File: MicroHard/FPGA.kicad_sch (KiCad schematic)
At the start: 0 parts

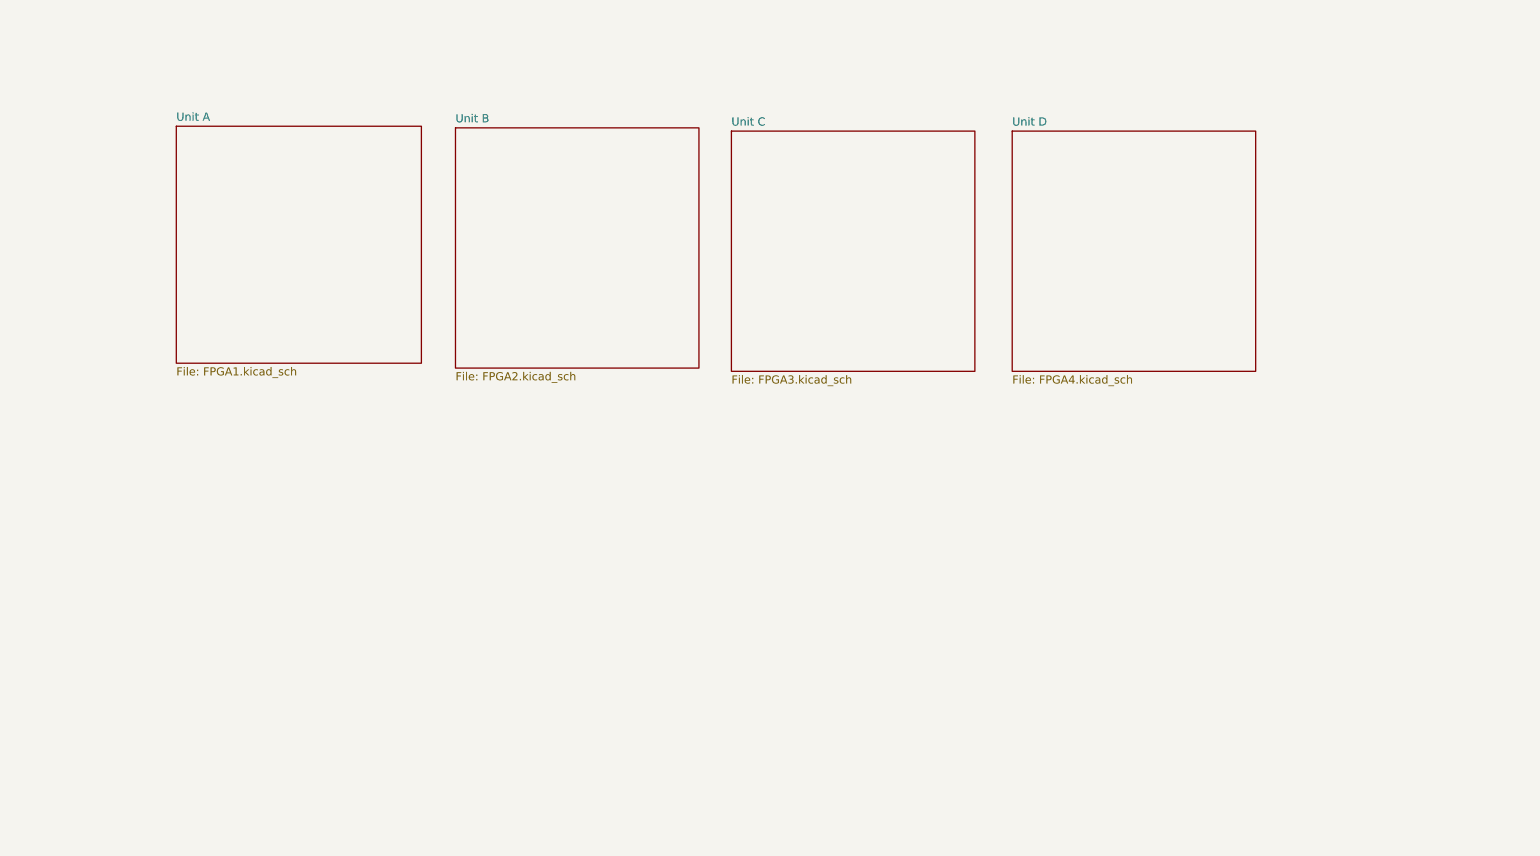
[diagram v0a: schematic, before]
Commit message: feat: finished FPGA config
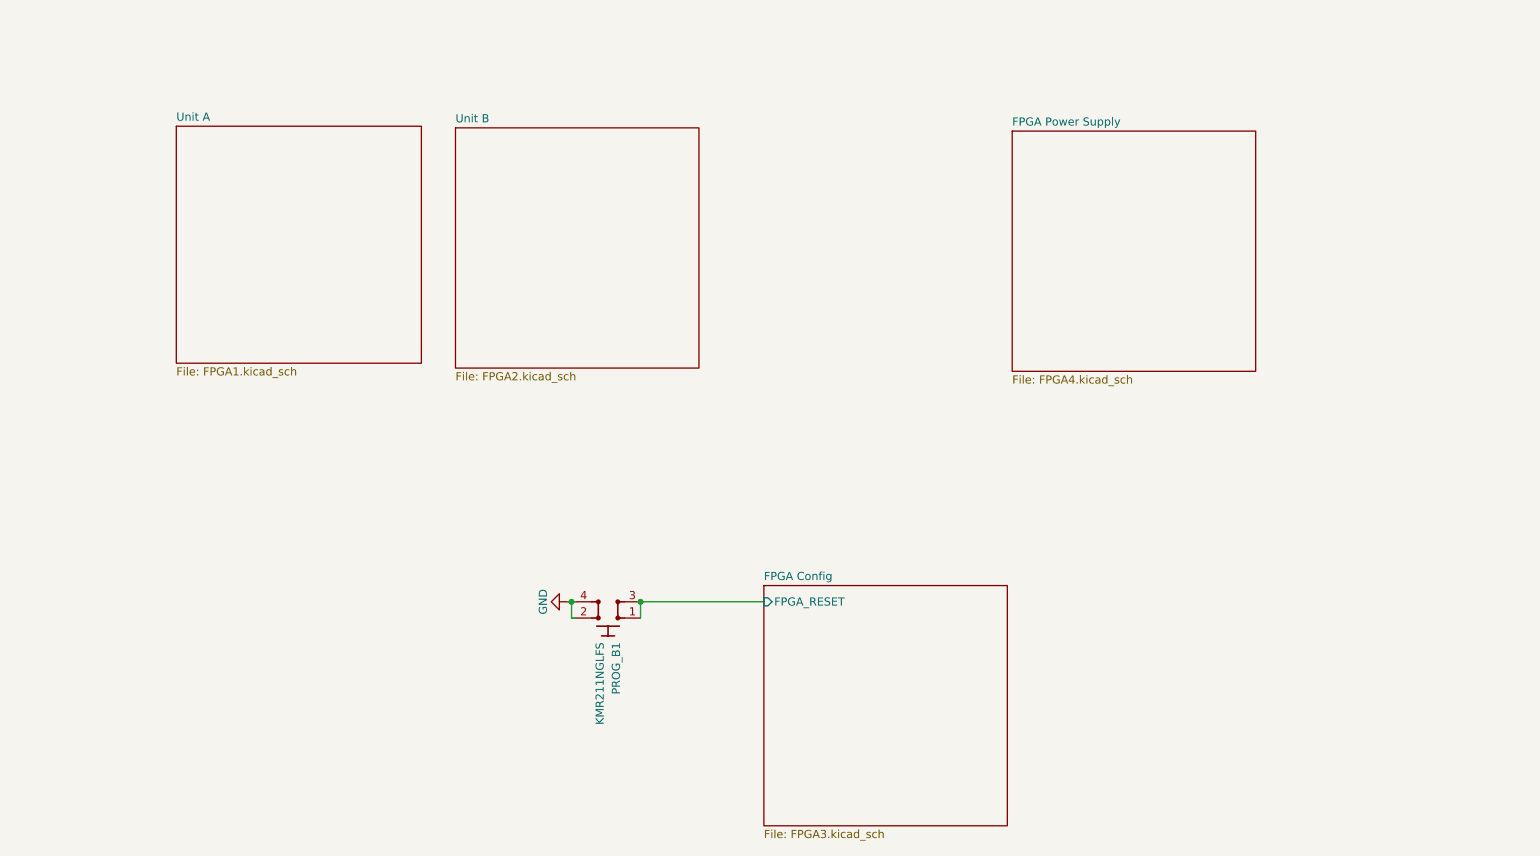
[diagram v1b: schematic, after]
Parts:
- added PROG_B1: SW_SPST_KMR211NGLFS, antmicro-footprints:SW_SPST_4.2x2.8, symbol antmicroPushbuttonSwitches:SW_SPST_KMR211NGLFS
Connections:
- new net FPGA Config/FPGA_RESET: PROG_B1.1, PROG_B1.3
- new net GND: PROG_B1.2, PROG_B1.4
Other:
- sheet Unit C renamed FPGA Config
- sheet Unit D renamed FPGA Power Supply
- sheet FPGA Config ports: added FPGA_RESET; removed none

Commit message: feat: finished Flash mem and FPGA Config
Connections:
- net FPGA Config/FPGA_RESET renamed FPGA_RESET
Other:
- sheet FPGA Config ports: added FPGA_CONFIG_CLOCK; removed none
- sheet Unit A ports: added FPGA_CONFIG_CLOCK; removed none
- note added: "Active Low Full Chip Reset"
- moved on the sheet: PROG_B1
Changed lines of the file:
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@@
 	(paper "A4")
 	(junction
-		(at 94.615 115.57)
+		(at 46.99 113.03)
 		(diameter 0)
 		(color 0 0 0 0)
 	)
 	(junction
-		(at 105.41 115.57)
+		(at 26.035 113.03)
 		(diameter 0)
 		(color 0 0 0 0)
 	)
-	(wire
-		(pts
-			(xy 94.615 118.11) (xy 95.25 118.11)
-		)
-		(stroke
-			(width 0)
-			(type default)
-		)
-	)
-	(wire
-		(pts
-			(xy 94.615 115.57) (xy 95.25 115.57)
-		)
-		(stroke
-			(width 0)
-			(type default)
-		)
-	)
-	(wire
-		(pts
-			(xy 105.41 115.57) (xy 124.714 115.57)
-		)
-		(stroke
-			(width 0)
-			(type default)
-		)
-	)
-	(wire
-		(pts
-			(xy 105.41 115.57) (xy 105.41 118.11)
-		)
-		(stroke
-			(width 0)
-			(type default)
-		)
-	)
-	(wire
-		(pts
-			(xy 94.615 118.11) (xy 94.615 115.57)
-		)
-		(stroke
-			(width 0)
-			(type default)
-		)
-	)
-	(wire
-		(pts
-			(xy 94.615 115.57) (xy 93.98 115.57)
-		)
-		(stroke
-			(width 0)
-			(type default)
+	(junction
+		(at 36.83 113.03)
+		(diameter 0)
+		(color 0 0 0 0)
+	)
+	(junction
+		(at 115.316 114.3)
+		(diameter 0)
+		(color 0 0 0 0)
+	)
+	(wire
+		(pts
+			(xy 57.15 113.03) (xy 46.99 113.03)
+		)
+		(stroke
+			(width 0)
+			(type default)
+		)
+	)
+	(wire
+		(pts
+			(xy 26.035 115.57) (xy 26.67 115.57)
+		)
+		(stroke
+			(width 0)
+			(type default)
+		)
+	)
+	(wire
+		(pts
+			(xy 26.035 113.03) (xy 26.67 113.03)
+		)
+		(stroke
+			(width 0)
+			(type default)
+		)
+	)
+	(wire
+		(pts
+			(xy 36.83 113.03) (xy 46.99 113.03)
+		)
+		(stroke
+			(width 0)
+			(type default)
+		)
+	)
+	(wire
+		(pts
+			(xy 115.316 114.3) (xy 115.57 114.3)
+		)
+		(stroke
+			(width 0)
+			(type default)
+		)
+	)
+	(wire
+		(pts
+			(xy 46.99 105.41) (xy 46.99 113.03)
+		)
+		(stroke
+			(width 0)
+			(type default)
+		)
+	)
+	(wire
+		(pts
+			(xy 36.83 113.03) (xy 36.83 115.57)
+		)
+		(stroke
+			(width 0)
+			(type default)
+		)
+	)
+	(wire
+		(pts
+			(xy 95.25 114.3) (xy 115.316 114.3)
+		)
+		(stroke
+			(width 0)
+			(type default)
+		)
+	)
+	(wire
+		(pts
+			(xy 57.15 113.03) (xy 57.15 114.3)
+		)
+		(stroke
+			(width 0)
+			(type default)
+		)
+	)
+	(wire
+		(pts
+			(xy 26.035 115.57) (xy 26.035 113.03)
+		)
+		(stroke
+			(width 0)
+			(type default)
+		)
+	)
+	(wire
+		(pts
+			(xy 26.035 113.03) (xy 25.4 113.03)
+		)
+		(stroke
+			(width 0)
+			(type default)
+		)
+	)
+	(text "Active Low Full Chip Reset"
+		(exclude_from_sim no)
+		(at 62.484 98.552 0)
+		(effects
+			(font
+				(size 1.27 1.27)
+			)
+		)
+	)
+	(global_label "FPGA_RESET"
+		(shape input)
+		(at 46.99 105.41 90)
+		(fields_autoplaced yes)
+		(effects
+			(font
+				(size 1.27 1.27)
+			)
+			(justify left)
+		)
+		(property "Intersheetrefs" "${INTERSHEET_REFS}"
+			(at 46.99 90.9949 90)
+			(effects
+				(font
+					(size 1.27 1.27)
+				)
+				(justify left)
+				(hide yes)
+			)
 		)
 	)
 	(symbol
 		(lib_id "antmicroPushbuttonSwitches:SW_SPST_KMR211NGLFS")
-		(at 105.41 118.11 180)
+		(at 36.83 115.57 180)
 		(unit 1)
 		(exclude_from_sim no)
@@
 		(fields_autoplaced yes)
 		(property "Reference" "PROG_B1"
-			(at 101.6001 121.92 90)
+			(at 33.0201 119.38 90)
 			(effects
 				(font
@@
 		)
 		(property "Value" "SW_SPST_KMR211NGLFS"
-			(at 99.0601 121.92 90)
+			(at 30.4801 119.38 90)
 			(effects
 				(font
@@
 		)
 		(property "Footprint" "antmicro-footprints:SW_SPST_4.2x2.8"
-			(at 80.01 110.49 0)
+			(at 11.43 107.95 0)
 			(effects
 				(font
@@
 		)
 		(property "Datasheet" "http://www.farnell.com/datasheets/2631211.pdf"
-			(at 80.01 107.95 0)
+			(at 11.43 105.41 0)
 			(effects
 				(font
@@
 		)
 		(property "Description" ""
-			(at 105.41 118.11 0)
+			(at 36.83 115.57 0)
 			(effects
 				(font
@@
 		)
 		(property "MPN" "KMR211NGLFS"
-			(at 99.0601 121.92 90)
+			(at 30.4801 119.38 90)
 			(effects
 				(font
@@
 		)
 		(property "Manufacturer" "C&K"
-			(at 80.01 102.87 0)
+			(at 11.43 100.33 0)
 			(effects
 				(font
@@
 		)
 		(property "Author" "Antmicro"
-			(at 80.01 100.33 0)
+			(at 11.43 97.79 0)
 			(effects
 				(font
@@
 		)
 		(property "License" "Apache-2.0"
-			(at 80.01 97.79 0)
+			(at 11.43 95.25 0)
 			(effects
 				(font
@@
 	(symbol
 		(lib_id "antmicropower:GND")
-		(at 93.98 115.57 270)
+		(at 25.4 113.03 270)
 		(unit 1)
 		(exclude_from_sim no)
@@
 		(dnp no)
 		(property "Reference" "#PWR018"
-			(at 87.63 115.57 0)
+			(at 19.05 113.03 0)
 			(effects
 				(font
@@
 		)
 		(property "Value" "GND"
-			(at 90.17 115.57 0)
+			(at 21.59 113.03 0)
 			(effects
 				(font
@@
 		)
 		(property "Footprint" ""
-			(at 93.98 115.57 0)
+			(at 25.4 113.03 0)
 			(effects
 				(font
@@
 		)
 		(property "Datasheet" ""
-			(at 93.98 115.57 0)
+			(at 25.4 113.03 0)
 			(effects
 				(font
@@
 		)
 		(property "Description" ""
-			(at 93.98 115.57 0)
+			(at 25.4 113.03 0)
 			(effects
 				(font
@@
 		)
 		(property "Author" "Antmicro"
-			(at 86.36 124.46 0)
+			(at 17.78 121.92 0)
 			(effects
 				(font
@@
 		)
 		(property "License" "Apache-2.0"
-			(at 83.82 124.46 0)
+			(at 15.24 121.92 0)
 			(effects
 				(font
@@
 	)
 	(sheet
-		(at 32.766 41.148)
+		(at 115.316 112.268)
 		(size 38.354 37.084)
 		(fields_autoplaced yes)
@@
 		)
 		(property "Sheetname" "Unit A"
-			(at 32.766 40.4364 0)
+			(at 115.316 111.5564 0)
 			(effects
 				(font
@@
 		)
 		(property "Sheetfile" "FPGA1.kicad_sch"
-			(at 32.766 78.8166 0)
+			(at 115.316 149.9366 0)
 			(effects
 				(font
@@
 				)
 				(justify left top)
+			)
+		)
+		(pin "FPGA_CONFIG_CLOCK" input
+			(at 115.316 114.3 180)
+			(effects
+				(font
+					(size 1.27 1.27)
+				)
+				(justify left)
 			)
 		)
@@
 	)
 	(sheet
-		(at 124.714 113.03)
+		(at 57.15 111.76)
 		(size 38.1 37.592)
 		(fields_autoplaced yes)
@@
 		)
 		(property "Sheetname" "FPGA Config"
-			(at 124.714 112.3184 0)
+			(at 57.15 111.0484 0)
 			(effects
 				(font
@@
 		)
 		(property "Sheetfile" "FPGA3.kicad_sch"
-			(at 124.714 151.2066 0)
+			(at 57.15 149.9366 0)
 			(effects
 				(font
@@
 		)
 		(pin "FPGA_RESET" input
-			(at 124.714 115.57 180)
-			(effects
-				(font
-					(size 1.27 1.27)
-				)
-				(justify left)
-			)
-		)
+			(at 57.15 114.3 180)
+			(effects
+				(font
+					(size 1.27 1.27)
+				)
+				(justify left)
+			)
+		)
+		(pin "FPGA_CONFIG_CLOCK" input
+			(at 95.25 114.3 0)
+			(effects
+				(font
+					(size 1.27 1.27)
+				)
+				(justify right)
+			)
+		)

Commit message: feat: finished config
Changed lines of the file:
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@@
 		(color 0 0 0 0)
 	)
-	(junction
-		(at 115.316 114.3)
-		(diameter 0)
-		(color 0 0 0 0)
-	)
 	(wire
 		(pts
@@
 	(wire
 		(pts
-			(xy 115.316 114.3) (xy 115.57 114.3)
+			(xy 95.25 147.32) (xy 205.74 147.32)
 		)
 		(stroke
@@
 		(pts
 			(xy 36.83 113.03) (xy 36.83 115.57)
-		)
-		(stroke
-			(width 0)
-			(type default)
-		)
-	)
-	(wire
-		(pts
-			(xy 95.25 114.3) (xy 115.316 114.3)
 		)
 		(stroke
@@
 	)
 	(sheet
-		(at 115.316 112.268)
+		(at 205.74 112.268)
 		(size 38.354 37.084)
 		(fields_autoplaced yes)
@@
 		)
 		(property "Sheetname" "Unit A"
-			(at 115.316 111.5564 0)
+			(at 205.74 111.5564 0)
 			(effects
 				(font
@@
 		)
 		(property "Sheetfile" "FPGA1.kicad_sch"
-			(at 115.316 149.9366 0)
+			(at 205.74 149.9366 0)
 			(effects
 				(font
@@
 		)
 		(pin "FPGA_CONFIG_CLOCK" input
-			(at 115.316 114.3 180)
+			(at 205.74 147.32 180)
 			(effects
 				(font
@@
 	)
 	(sheet
-		(at 76.454 41.402)
+		(at 56.134 26.162)
 		(size 38.1 37.592)
 		(fields_autoplaced yes)
@@
 		)
 		(property "Sheetname" "Unit B"
-			(at 76.454 40.6904 0)
+			(at 56.134 25.4504 0)
 			(effects
 				(font
@@
 		)
 		(property "Sheetfile" "FPGA2.kicad_sch"
-			(at 76.454 79.5786 0)
+			(at 56.134 64.3386 0)
 			(effects
 				(font
@@
 		)
 		(pin "FPGA_CONFIG_CLOCK" input
-			(at 95.25 114.3 0)
+			(at 95.25 147.32 0)
 			(effects
 				(font
@@
 	)
 	(sheet
-		(at 163.576 41.91)
+		(at 205.486 29.21)
 		(size 38.1 37.592)
 		(fields_autoplaced yes)
@@
 		)
 		(property "Sheetname" "FPGA Power Supply"
-			(at 163.576 41.1984 0)
+			(at 205.486 28.4984 0)
 			(effects
 				(font
@@
 		)
 		(property "Sheetfile" "FPGA4.kicad_sch"
-			(at 163.576 80.0866 0)
-			(effects
-				(font
+			(at 205.486 67.3866 0)
+			(effects
+				(font

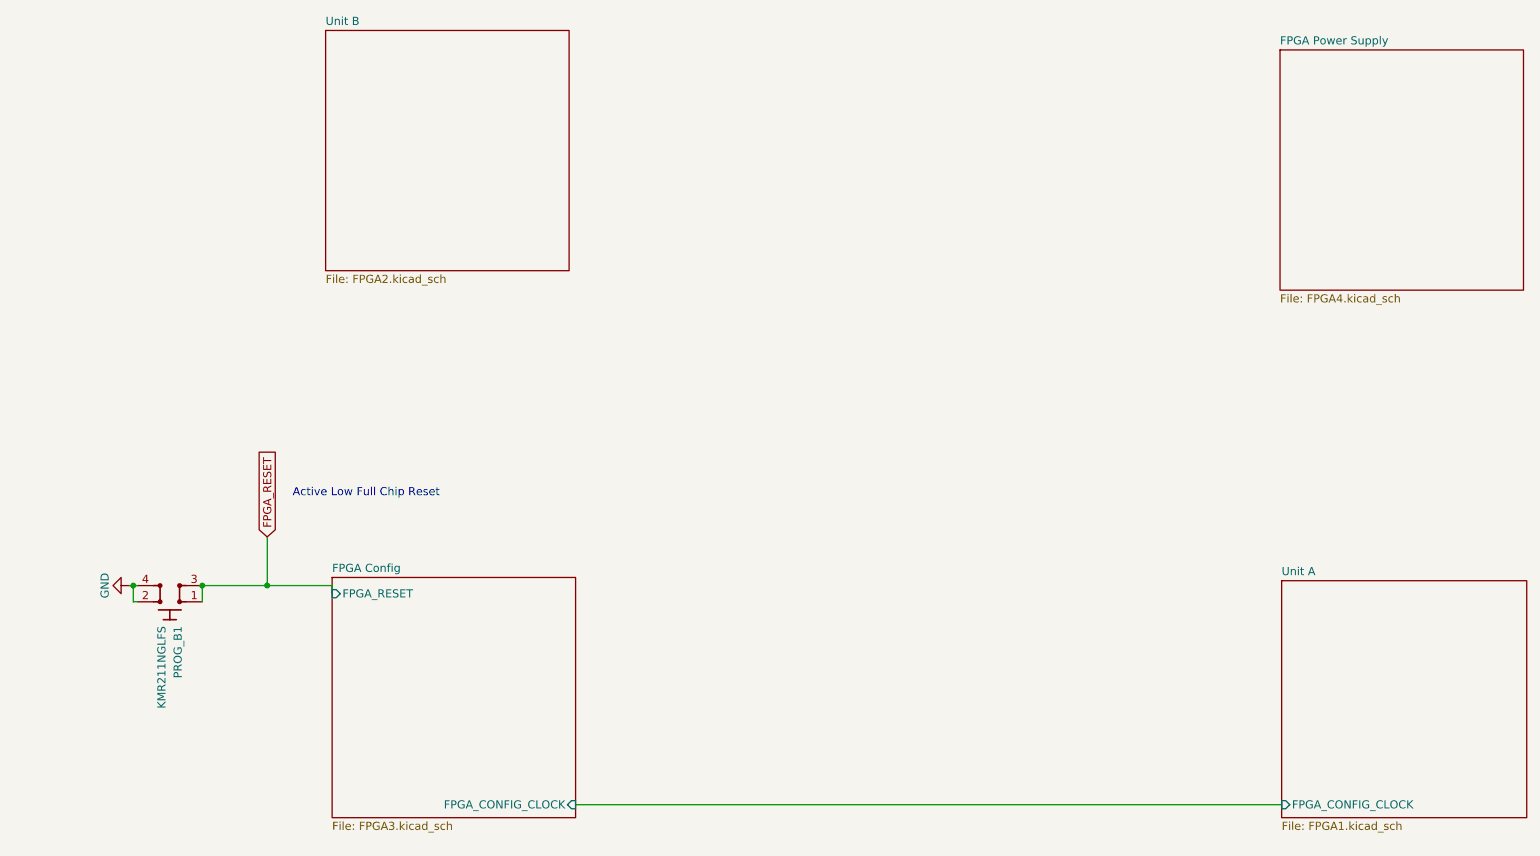
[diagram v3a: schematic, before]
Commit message: feat: added VGA signal out from FPGA
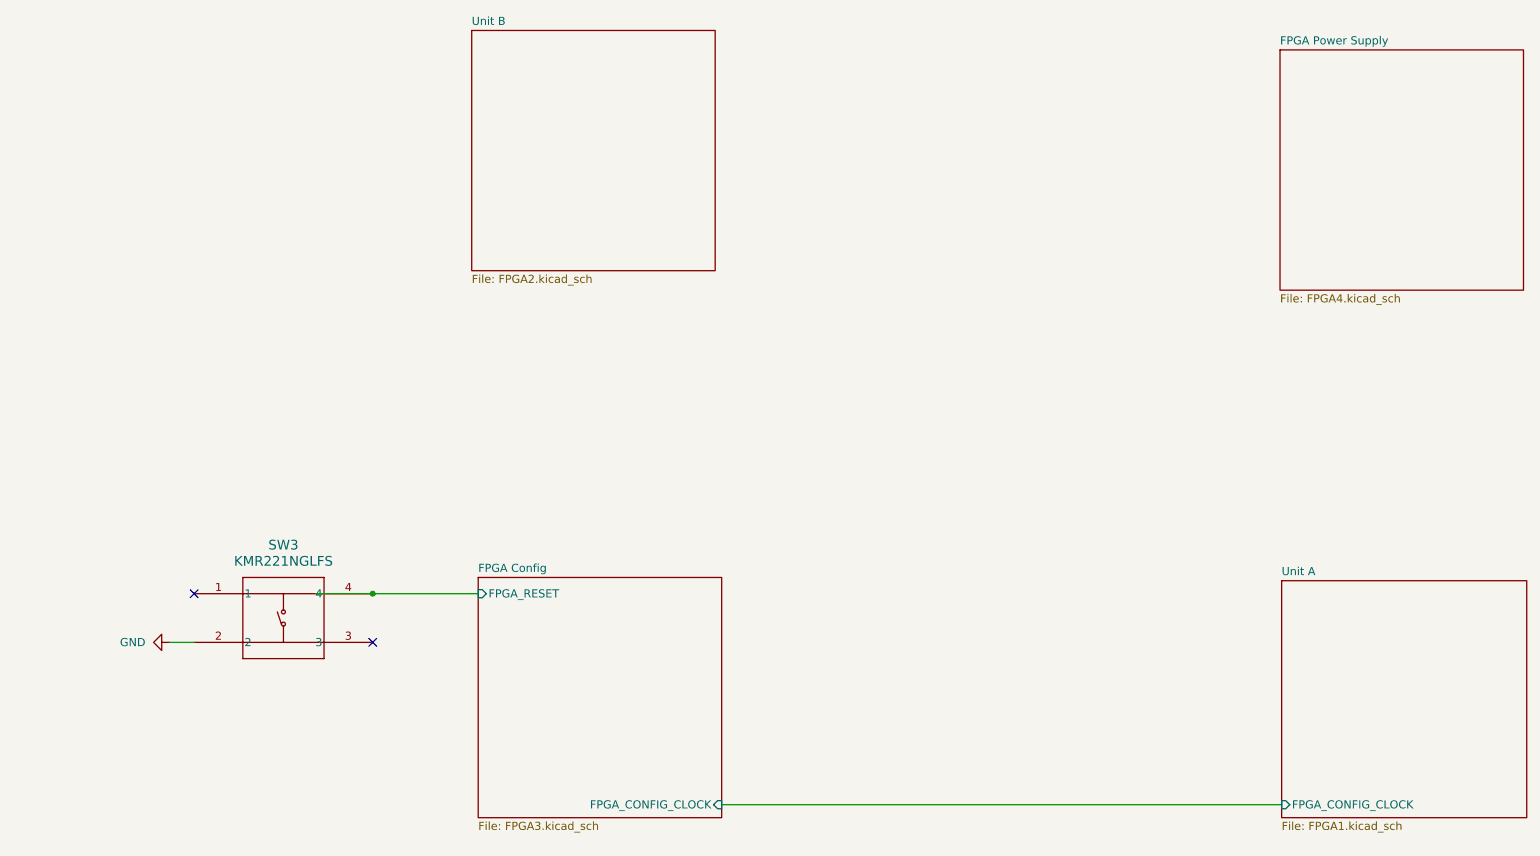
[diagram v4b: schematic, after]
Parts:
- removed PROG_B1: SW_SPST_KMR211NGLFS, antmicro-footprints:SW_SPST_4.2x2.8, symbol antmicroPushbuttonSwitches:SW_SPST_KMR211NGLFS
- added SW3: KMR221NGLFS, KMR221_CNK, symbol Button:KMR221NGLFS
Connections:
- net GND: now also SW3.2
- new net FPGA Config/FPGA_RESET: SW3.4
- no-connect marks 0 -> 2
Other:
- note removed: "Active Low Full Chip Reset"
